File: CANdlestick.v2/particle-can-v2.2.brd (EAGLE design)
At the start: 31.8 x 37.8 mm, 16 parts, among them IC1 LM2940, IC2 TJA1049, J1 OBDII

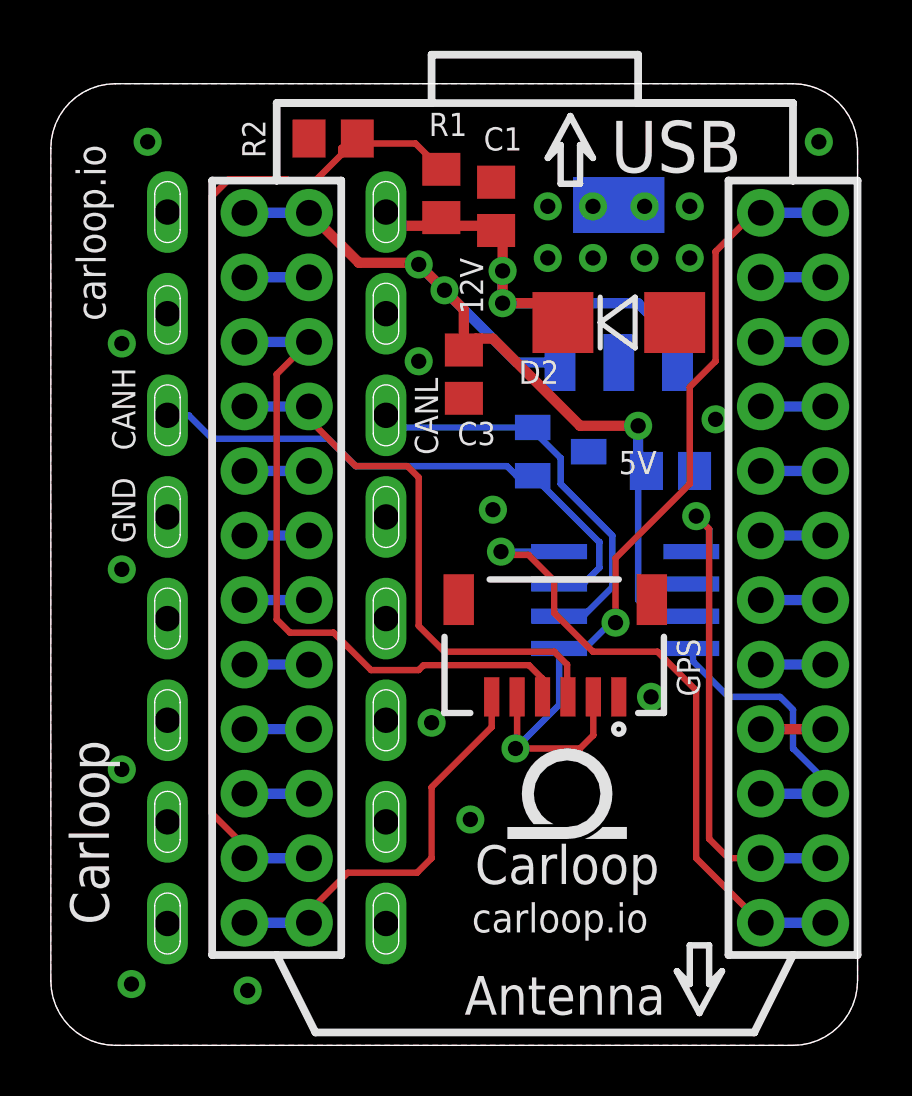
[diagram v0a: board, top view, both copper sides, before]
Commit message: Carloop PCB revision 2.2
- Flip the GPS connector landing pattern
- Add 2nd header to BOM
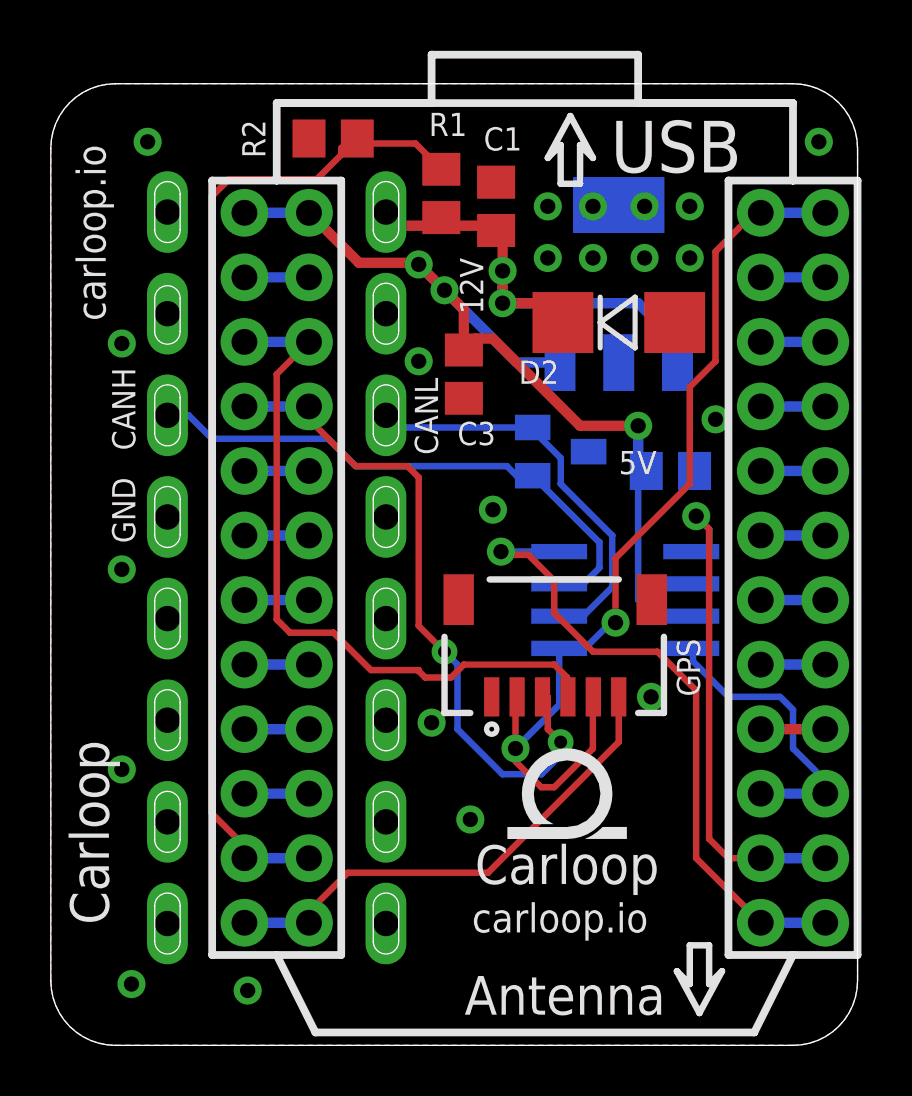
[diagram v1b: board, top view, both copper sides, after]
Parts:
- GPS: value JST_VERTICALHORIZONTAL -> JSTHORIZONTAL
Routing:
- net GPS_TX: track 21.9 -> 26.7 mm, vias 0 -> 2
- net GPS_EN: track 16.0 -> 19.8 mm
- net 3.3V: track 35.5 -> 37.5 mm
- net GPS_RX: track 26.3 -> 27.6 mm
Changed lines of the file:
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@@
 <element name="CORE" library="MuniRent" package="PHOTON_STACKABLE_EXTERNAL" value="PHOTONWITH_EXTERNAL_HEADERS" x="9.652" y="0.254" smashed="yes">
 <attribute name="VALUE" x="19.812" y="-15.621" size="1.27" layer="27" rot="R180"/>
-<attribute name="PARTNO" value="PPPC122LFBN-RC" x="9.652" y="0.254" size="1.778" layer="27" display="off"/>
+<attribute name="PARTNO" value="*" x="9.652" y="0.254" size="1.778" layer="27" display="off"/>
+<attribute name="BOM" value="EXCLUDE" x="9.652" y="0.254" size="1.778" layer="27" display="off"/>
 </element>
 <element name="IC2" library="MuniRent" package="SO8" value="TJA1049" x="23.368" y="17.272" smashed="yes" rot="MR270">
@@
 <attribute name="PARTNO" value="TJA1049T-118" x="23.368" y="17.272" size="1.778" layer="28" rot="MR270" display="off"/>
 </element>
-<element name="GPS" library="MuniRent" package="JST-6-SMD-HOR-1.0MM" value="JST_VERTICALHORIZONTAL" x="20.574" y="14.732" smashed="yes" rot="R180">
+<element name="GPS" library="MuniRent" package="JST-6-SMD-HOR-1.0MM" value="JSTHORIZONTAL" x="20.574" y="14.732" smashed="yes" rot="R180">
 <attribute name="NAME" x="25.4" y="15.748" size="0.9144" layer="25" font="vector" ratio="16" rot="R270"/>
 <attribute name="VALUE" x="21.844" y="17.272" size="0.4064" layer="27" rot="R180"/>
@@
 <wire x1="20.828" y1="15.494" x2="20.828" y2="15.427" width="0.254" layer="16"/>
 <wire x1="20.828" y1="15.427" x2="20.768" y2="15.367" width="0.254" layer="16"/>
-<wire x1="19.114" y1="13.462" x2="19.114" y2="11.494" width="0.254" layer="1"/>
 <wire x1="19.114" y1="11.494" x2="19.05" y2="11.43" width="0.254" layer="1"/>
-<wire x1="22.114" y1="13.462" x2="22.114" y2="11.954" width="0.254" layer="1"/>
-<wire x1="22.114" y1="11.954" x2="21.59" y2="11.43" width="0.254" layer="1"/>
-<wire x1="21.59" y1="11.43" x2="19.05" y2="11.43" width="0.254" layer="1"/>
 <wire x1="20.768" y1="15.367" x2="20.768" y2="13.148" width="0.254" layer="16"/>
 <wire x1="20.768" y1="13.148" x2="19.05" y2="11.43" width="0.254" layer="16"/>
 <wire x1="22.987" y1="16.383" x2="22.7965" y2="16.383" width="0.254" layer="16"/>
 <wire x1="22.7965" y1="16.383" x2="21.7805" y2="15.367" width="0.254" layer="16"/>
+<wire x1="19.05" y1="11.43" x2="19.05" y2="13.462" width="0.254" layer="1"/>
+<wire x1="19.05" y1="13.462" x2="19.114" y2="13.462" width="0.254" layer="1"/>
+<wire x1="22.098" y1="11.43" x2="22.098" y2="13.462" width="0.254" layer="1"/>
+<wire x1="20.574" y1="9.906" x2="22.098" y2="11.43" width="0.254" layer="1"/>
+<wire x1="20.066" y1="9.906" x2="20.574" y2="9.906" width="0.254" layer="1"/>
+<wire x1="19.05" y1="10.922" x2="20.066" y2="9.906" width="0.254" layer="1"/>
+<wire x1="19.05" y1="11.43" x2="19.05" y2="10.922" width="0.254" layer="1"/>
+<wire x1="22.098" y1="13.462" x2="22.114" y2="13.462" width="0.254" layer="1"/>
 </signal>
 <signal name="5V">
@@
 <wire x1="15.24" y1="22.098" x2="15.24" y2="16.256" width="0.254" layer="1"/>
 <wire x1="15.24" y1="16.256" x2="16.256" y2="15.24" width="0.254" layer="1"/>
-<wire x1="16.256" y1="15.24" x2="20.574" y2="15.24" width="0.254" layer="1"/>
-<wire x1="20.574" y1="15.24" x2="21.082" y2="14.732" width="0.254" layer="1"/>
-<wire x1="21.082" y1="14.732" x2="21.082" y2="13.494" width="0.254" layer="1"/>
-<wire x1="21.082" y1="13.494" x2="21.114" y2="13.462" width="0.254" layer="1"/>
+<wire x1="20.828" y1="11.684" x2="20.32" y2="12.192" width="0.254" layer="1"/>
+<wire x1="20.32" y1="12.192" x2="20.32" y2="13.462" width="0.254" layer="1"/>
+<wire x1="20.066" y1="10.414" x2="20.828" y2="11.176" width="0.254" layer="16"/>
+<wire x1="20.828" y1="11.176" x2="20.828" y2="11.684" width="0.254" layer="16"/>
+<wire x1="18.542" y1="10.414" x2="20.066" y2="10.414" width="0.254" layer="16"/>
+<wire x1="16.764" y1="12.192" x2="18.542" y2="10.414" width="0.254" layer="16"/>
+<wire x1="16.764" y1="14.732" x2="16.764" y2="12.192" width="0.254" layer="16"/>
+<wire x1="16.256" y1="15.24" x2="16.764" y2="14.732" width="0.254" layer="16"/>
+<wire x1="20.32" y1="13.462" x2="20.114" y2="13.462" width="0.254" layer="1"/>
+<via x="20.828" y="11.684" extent="1-16" drill="0.508"/>
+<via x="16.256" y="15.24" extent="1-16" drill="0.508"/>
 </signal>
 <signal name="GPS_RX">
@@
 <wire x1="9.652" y1="26.162" x2="9.652" y2="16.51" width="0.254" layer="1"/>
 <wire x1="9.652" y1="16.51" x2="10.1727" y2="15.9893" width="0.254" layer="1"/>
-<wire x1="20.114" y1="13.462" x2="20.114" y2="14.176" width="0.254" layer="1"/>
 <wire x1="13.3604" y1="14.5161" x2="15.24" y2="14.5161" width="0.254" layer="1"/>
-<wire x1="19.5834" y1="14.7066" x2="20.114" y2="14.176" width="0.254" layer="1"/>
 <wire x1="13.3604" y1="14.5161" x2="11.8872" y2="15.9893" width="0.254" layer="1"/>
 <wire x1="10.1727" y1="15.9893" x2="11.8872" y2="15.9893" width="0.254" layer="1"/>
-<wire x1="19.5834" y1="14.7066" x2="15.4305" y2="14.7066" width="0.254" layer="1"/>
-<wire x1="15.4305" y1="14.7066" x2="15.24" y2="14.5161" width="0.254" layer="1"/>
+<wire x1="21.082" y1="14.224" x2="21.082" y2="13.462" width="0.254" layer="1"/>
+<wire x1="20.574" y1="14.732" x2="21.082" y2="14.224" width="0.254" layer="1"/>
+<wire x1="17.018" y1="14.732" x2="20.574" y2="14.732" width="0.254" layer="1"/>
+<wire x1="16.51" y1="14.224" x2="17.018" y2="14.732" width="0.254" layer="1"/>
+<wire x1="15.494" y1="14.224" x2="16.51" y2="14.224" width="0.254" layer="1"/>
+<wire x1="15.24" y1="14.478" x2="15.494" y2="14.224" width="0.254" layer="1"/>
+<wire x1="21.082" y1="13.462" x2="21.114" y2="13.462" width="0.254" layer="1"/>
+<wire x1="15.24" y1="14.478" x2="15.24" y2="14.5161" width="0.254" layer="1"/>
 </signal>
 <signal name="GPS_EN">
@@
 <wire x1="10.922" y1="4.572" x2="8.382" y2="4.572" width="0.4064" layer="16"/>
 <wire x1="10.922" y1="5.08" x2="10.922" y2="4.572" width="0.254" layer="1"/>
-<wire x1="12.446" y1="6.5405" x2="15.1765" y2="6.5405" width="0.254" layer="1"/>
-<wire x1="15.1765" y1="6.5405" x2="15.748" y2="7.112" width="0.254" layer="1"/>
-<wire x1="15.748" y1="7.112" x2="15.748" y2="9.906" width="0.254" layer="1"/>
-<wire x1="15.748" y1="9.906" x2="18.114" y2="12.272" width="0.254" layer="1"/>
-<wire x1="18.114" y1="13.462" x2="18.114" y2="12.272" width="0.254" layer="1"/>
 <wire x1="10.922" y1="5.08" x2="10.9855" y2="5.08" width="0.254" layer="1"/>
 <wire x1="10.9855" y1="5.08" x2="12.446" y2="6.5405" width="0.254" layer="1"/>
+<wire x1="23.114" y1="11.684" x2="23.114" y2="13.462" width="0.254" layer="1"/>
+<wire x1="12.446" y1="6.5405" x2="17.9705" y2="6.5405" width="0.254" layer="1"/>
+<wire x1="17.9705" y1="6.5405" x2="23.114" y2="11.684" width="0.254" layer="1"/>
 </signal>
 <signal name="VBAT">
@@
 <wire x1="12.192" y1="35.052" x2="12.7" y2="35.56" width="0.254" layer="1"/>
 <wire x1="12.192" y1="34.798" x2="12.192" y2="35.052" width="0.254" layer="1"/>
-<wire x1="11.176" y1="33.782" x2="12.192" y2="34.798" width="0.254" layer="1"/>
-<wire x1="10.16" y1="33.782" x2="11.176" y2="33.782" width="0.254" layer="1"/>
 <wire x1="13.0175" y1="35.24" x2="15.113" y2="35.24" width="0.254" layer="1"/>
 <wire x1="15.113" y1="35.24" x2="16.129" y2="34.224" width="0.254" layer="1"/>
@@
 <wire x1="7.0866" y1="33.147" x2="7.0866" y2="8.89" width="0.254" layer="1"/>
 <wire x1="7.7724" y1="33.8328" x2="7.0866" y2="33.147" width="0.254" layer="1"/>
-<wire x1="10.0584" y1="33.8328" x2="7.7724" y2="33.8328" width="0.254" layer="1"/>
+<wire x1="10.0584" y1="33.8328" x2="9.906" y2="33.8328" width="0.254" layer="1"/>
+<wire x1="9.906" y1="33.8328" x2="7.7724" y2="33.8328" width="0.254" layer="1"/>
 <wire x1="13.0175" y1="35.24" x2="12.8245" y2="35.433" width="0.4064" layer="1"/>
 <wire x1="8.382" y1="7.112" x2="8.382" y2="7.1628" width="0.254" layer="1"/>
 <wire x1="8.382" y1="7.1628" x2="8.2296" y2="7.3152" width="0.254" layer="1"/>
+<wire x1="12.192" y1="34.798" x2="11.2268" y2="33.8328" width="0.254" layer="1"/>
+<wire x1="11.2268" y1="33.8328" x2="10.0584" y2="33.8328" width="0.254" layer="1"/>
 <wire x1="12.7" y1="35.56" x2="12.8245" y2="35.433" width="0" layer="19" extent="1-1"/>
-<wire x1="10.0584" y1="33.8328" x2="10.16" y2="33.782" width="0" layer="19" extent="1-1"/>
 </signal>
 <signal name="GND1">
